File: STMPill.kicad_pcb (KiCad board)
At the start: 4 copper layers, 40 x 55.5 mm, 65 parts, among them J1 Conn_Coaxial, J2 TC2030, J3 USB_C_16P, J4 Conn_01x20_L, J5 Conn_01x20_R, Q1 SS8550, Q3 SS8050, SW1 SW_Push, SW2 SW_Push, U1 STM32WB55REVx, U2 CP2102N-Axx-xQFN24, U3 TPS78233DDC, U4 USBLC6-2SC6, X1 32MHz, Y1 32.768kHz

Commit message: saving
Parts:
- moved C1 2.23 mm to (103.7, 88.3)
- moved C4 2.23 mm to (103.7, 87.7)
- moved C17 0.92 mm to (105.0, 86.2)
- moved C18 0.92 mm to (105.0, 87.0)
- moved D6 0.21 mm to (119.8, 98.5)
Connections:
- J4 pad 1: /PC12 -> +3.3V
- J4 pad 2: /PD0 -> +3.3V
- J4 pad 3: /PD1 -> GND
- J4 pad 4: /PB4 -> GND
- J4 pad 5: /PB5 -> /PD1
- J4 pad 6: /PB6 -> /PB4
- J5 pad 1: GND -> +5V
- J5 pad 2: +3.3V -> GND
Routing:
- net /PC11: track 0.00 -> 44.4 mm, vias 0 -> 1
- net /PC10: track 0.00 -> 40.9 mm, vias 0 -> 1
- net /PA15: track 0.00 -> 37.4 mm, vias 0 -> 1
- net /PD1: track 0.00 -> 33.0 mm, vias 0 -> 3
- net /PB4: track 0.00 -> 31.5 mm, vias 0 -> 3
- net /PA12: track 0.00 -> 31.1 mm, vias 0 -> 1
- net /PB8: track 0.00 -> 28.4 mm, vias 0 -> 3
- net /PA11: track 0.00 -> 28.2 mm, vias 0 -> 1
- net /PB7: track 0.00 -> 27.9 mm, vias 0 -> 3
- net /PC13: track 0.00 -> 26.9 mm, vias 0 -> 3
- net /PC6: track 0.00 -> 23.4 mm
- net /PB15: track 0.00 -> 21.3 mm
- net /PE4: track 0.00 -> 21.3 mm
- net /PB14: track 0.00 -> 19.4 mm
- net /PB1: track 0.00 -> 19.1 mm
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
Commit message: touchups
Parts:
- added FID1: Fiducial, Fiducial:Fiducial_0.5mm_Mask1mm, F.Cu at (101.0, 73.0)
- added FID2: Fiducial, Fiducial:Fiducial_0.5mm_Mask1mm, F.Cu at (103.6, 123.3)
- added FID3: Fiducial, Fiducial:Fiducial_0.5mm_Mask1mm, F.Cu at (118.5, 123.1)
- SW1, SW2: footprint jej:SW_PUSH_SMD,3x2mm -> easyeda2kicad:KEY-SMD_L3.9-W3.0-LS5.0-EH
- moved C3 1.38 mm to (112.0, 79.0), turned to 90 degrees
- moved R4 0.35 mm to (121.9, 115.9)
- moved R5 0.35 mm to (123.0, 115.9)
- moved D2 0.25 mm to (121.9, 114.4)
- moved D3 0.25 mm to (123.0, 114.3)
- moved C9 0.20 mm to (110.2, 80.2)
- moved L2 0.15 mm to (104.0, 84.1)
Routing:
- net /PC4: track 0.00 -> 31.3 mm, vias 0 -> 1
- net /PC5: track 0.00 -> 30.3 mm, vias 0 -> 1
- net /PB2: track 0.00 -> 29.5 mm, vias 0 -> 1
- net /PB10: track 0.00 -> 29.2 mm, vias 0 -> 1
- net /PB11: track 0.00 -> 28.8 mm, vias 0 -> 1
- net GND: track 31.1 -> 40.6 mm, vias 64 -> 201
- net +3.3V: track 28.1 -> 32.9 mm
- net /NRTS: track 1.51 -> 5.45 mm, vias 0 -> 2
- net /PB1: track 19.1 -> 20.6 mm
- net /PE4: track 21.3 -> 22.5 mm
- net /PA0: track 26.5 -> 27.2 mm
- net /PA1: track 24.7 -> 25.4 mm
- net /PA2: track 22.1 -> 22.7 mm
- net /PA3: track 20.2 -> 20.8 mm
- net /PA4: track 18.8 -> 19.4 mm
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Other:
- board text added: "3V3"
- board text added: "5V"
- board text added: "A0"
- board text added: "A1"
- board text added: "A11"
- board text added: "A12"
- board text added: "A15"
- board text added: "A2"
- board text added: "A3"
- board text added: "A4"
- board text added: "A5"
- board text added: "A6"
- board text added: "A7"
- board text added: "A8"
- board text added: "B0"
- board text added: "B1"
- board text added: "B10"
- board text added: "B11"
- board text added: "B12"
- board text added: "B13"
- board text added: "B14"
- board text added: "B15"
- board text added: "B2"
- board text added: "B4"
- board text added: "B7"
- board text added: "B8"
- board text added: "C10"
- board text added: "C11"
- board text added: "C13"
- board text added: "C2"
- board text added: "C3"
- board text added: "C4"
- board text added: "C5"
- board text added: "C6"
- board text added: "D1"
- board text added: "E4"
- board text added: "GND"

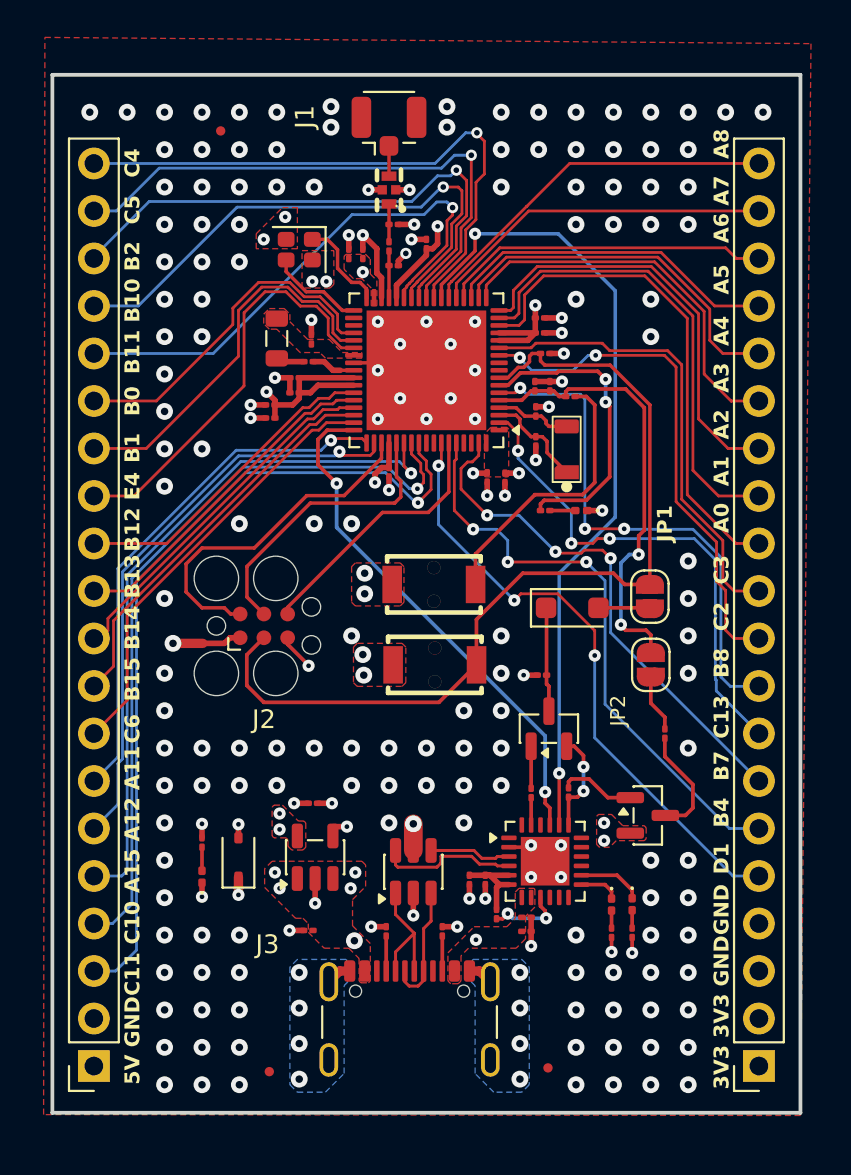
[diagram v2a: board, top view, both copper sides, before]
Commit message: fixing footprints
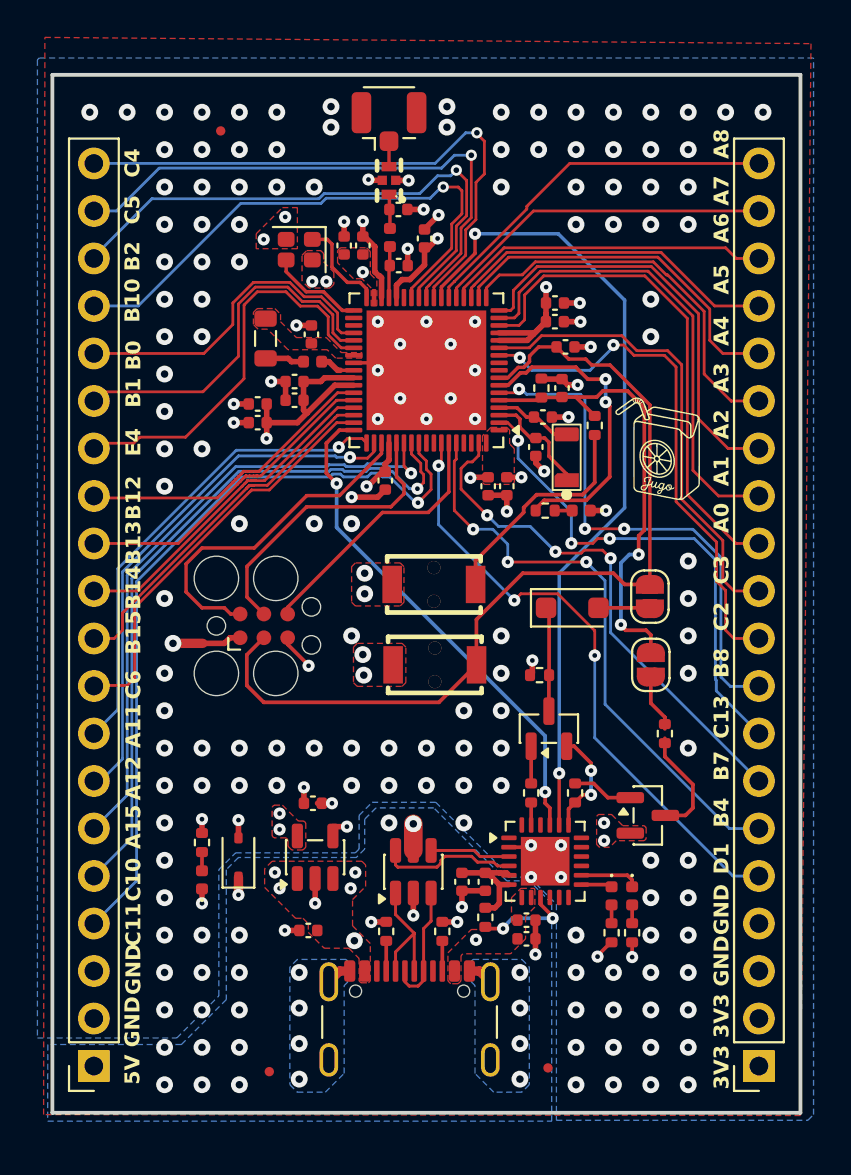
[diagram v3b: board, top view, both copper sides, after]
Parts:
- added G***: LOGO, LOGO, F.Cu at (124.5, 90.0)
- C1, C10, C11, C12, C13, C14, C15, C16, C17, C18, C19, C2, C20, C21, C22, C23, C24, C25, C3, C4, C5, C6, C7, C8, C9: footprint Capacitor_SMD:C_01005_0402Metric -> Capacitor_SMD:C_0402_1005Metric
- D1, D2, D3, D4: footprint LED_SMD:LED_0201_0603Metric -> Diode_SMD:D_0402_1005Metric
- L1, L3: footprint Inductor_SMD:L_01005_0402Metric -> Inductor_SMD:L_0402_1005Metric
- R1, R10, R11, R12, R13, R2, R3, R4, R5, R6, R7, R8, R9: footprint Resistor_SMD:R_01005_0402Metric -> Resistor_SMD:R_0402_1005Metric
- moved R1 2.02 mm to (121.0, 88.8), turned to 90 degrees
- moved C7 1.14 mm to (119.4, 84.5)
- moved C15 1.13 mm to (118.9, 82.2)
- moved C16 1.00 mm to (118.9, 83.2)
- moved C8 0.84 mm to (110.5, 77.2)
- moved C1 0.72 mm to (103.0, 88.6)
- moved C4 0.67 mm to (103.0, 87.6)
- moved C10 0.66 mm to (119.2, 86.8)
- moved R6 0.62 mm to (115.2, 115.0)
- moved L2 0.60 mm to (103.4, 84.1)
- moved C14 0.51 mm to (107.6, 79.1)
- moved FL1 0.51 mm to (110.0, 75.7)
- moved C5 0.49 mm to (109.8, 91.7)
- moved C12 0.48 mm to (118.2, 88.3), turned to 0 degrees
- moved C6 0.48 mm to (115.3, 92.0)
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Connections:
- J5 pad 10: /PB14 -> /PB15
- J5 pad 11: /PB13 -> /PB14
- J5 pad 12: /PB12 -> /PB13
- J5 pad 13: /PE4 -> /PB12
- J5 pad 14: /PB1 -> /PE4
- J5 pad 15: /PB0 -> /PB1
- J5 pad 16: /PB11 -> /PB0
- J5 pad 3: /PC11 -> GND
- J5 pad 4: /PC10 -> /PC11
- J5 pad 5: /PA15 -> /PC10
- J5 pad 6: /PA12 -> /PA15
- J5 pad 7: /PA11 -> /PA12
- J5 pad 8: /PC6 -> /PA11
- J5 pad 9: /PB15 -> /PC6
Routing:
- net /PB11: track 28.8 -> 0.00 mm, vias 1 -> 0
- net +3.3V: track 32.9 -> 37.6 mm
- net GND: track 40.6 -> 45.2 mm, vias 201 -> 198
- net /PA15: track 37.4 -> 34.0 mm
- net /PC11: track 44.4 -> 41.3 mm
- net /PC10: track 40.9 -> 37.8 mm
- net Net-(R1-Pad1): track 15.0 -> 12.1 mm
- net /PA11: track 28.2 -> 25.6 mm
- net /PA12: track 31.1 -> 28.7 mm
- net /PB15: track 21.3 -> 19.4 mm
- net /PC6: track 23.4 -> 21.9 mm
- net /PB14: track 19.4 -> 18.2 mm
- net Net-(U2-~{RST}): track 4.10 -> 5.28 mm
- net /PB13: track 18.1 -> 17.1 mm
- net Net-(U2-VDD): track 4.97 -> 6.02 mm
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- added copper zone on B.Cu, net +3.3V
- added copper zone on B.Cu, net +5V
- added copper zone on In2.Cu, net GND
- removed copper zone on In2.Cu, net +3.3V
- removed copper zone on In2.Cu, net +5V
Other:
- board text removed: "B11"
